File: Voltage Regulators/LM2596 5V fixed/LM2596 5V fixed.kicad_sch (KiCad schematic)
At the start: 5 parts, among them U1 LM2596S-5V

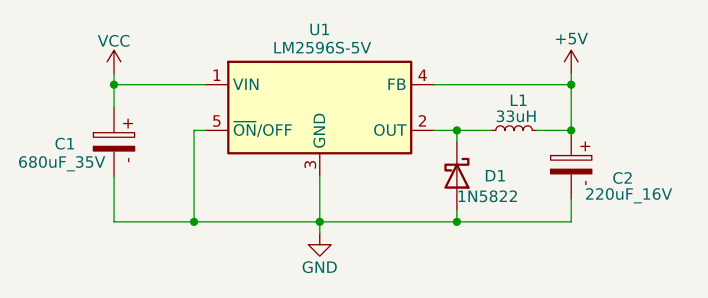
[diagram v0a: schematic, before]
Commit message: Edited 1N5822 to 1N5824
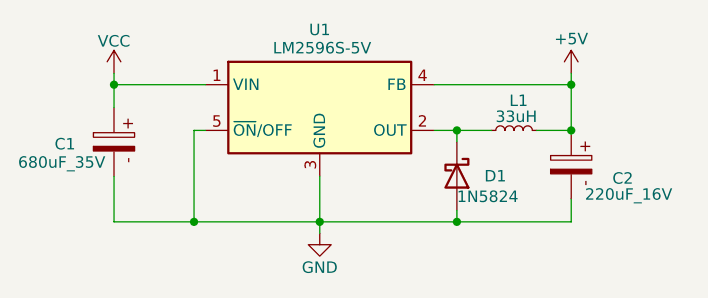
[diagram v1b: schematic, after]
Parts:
- D1: value 1N5822 -> 1N5824
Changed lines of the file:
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@@
 			)
 		)
-		(property "Value" "1N5822"
+		(property "Value" "1N5824"
 			(at 157.48 108.966 90)
 			(effects
